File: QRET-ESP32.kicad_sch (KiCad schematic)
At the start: 3 parts

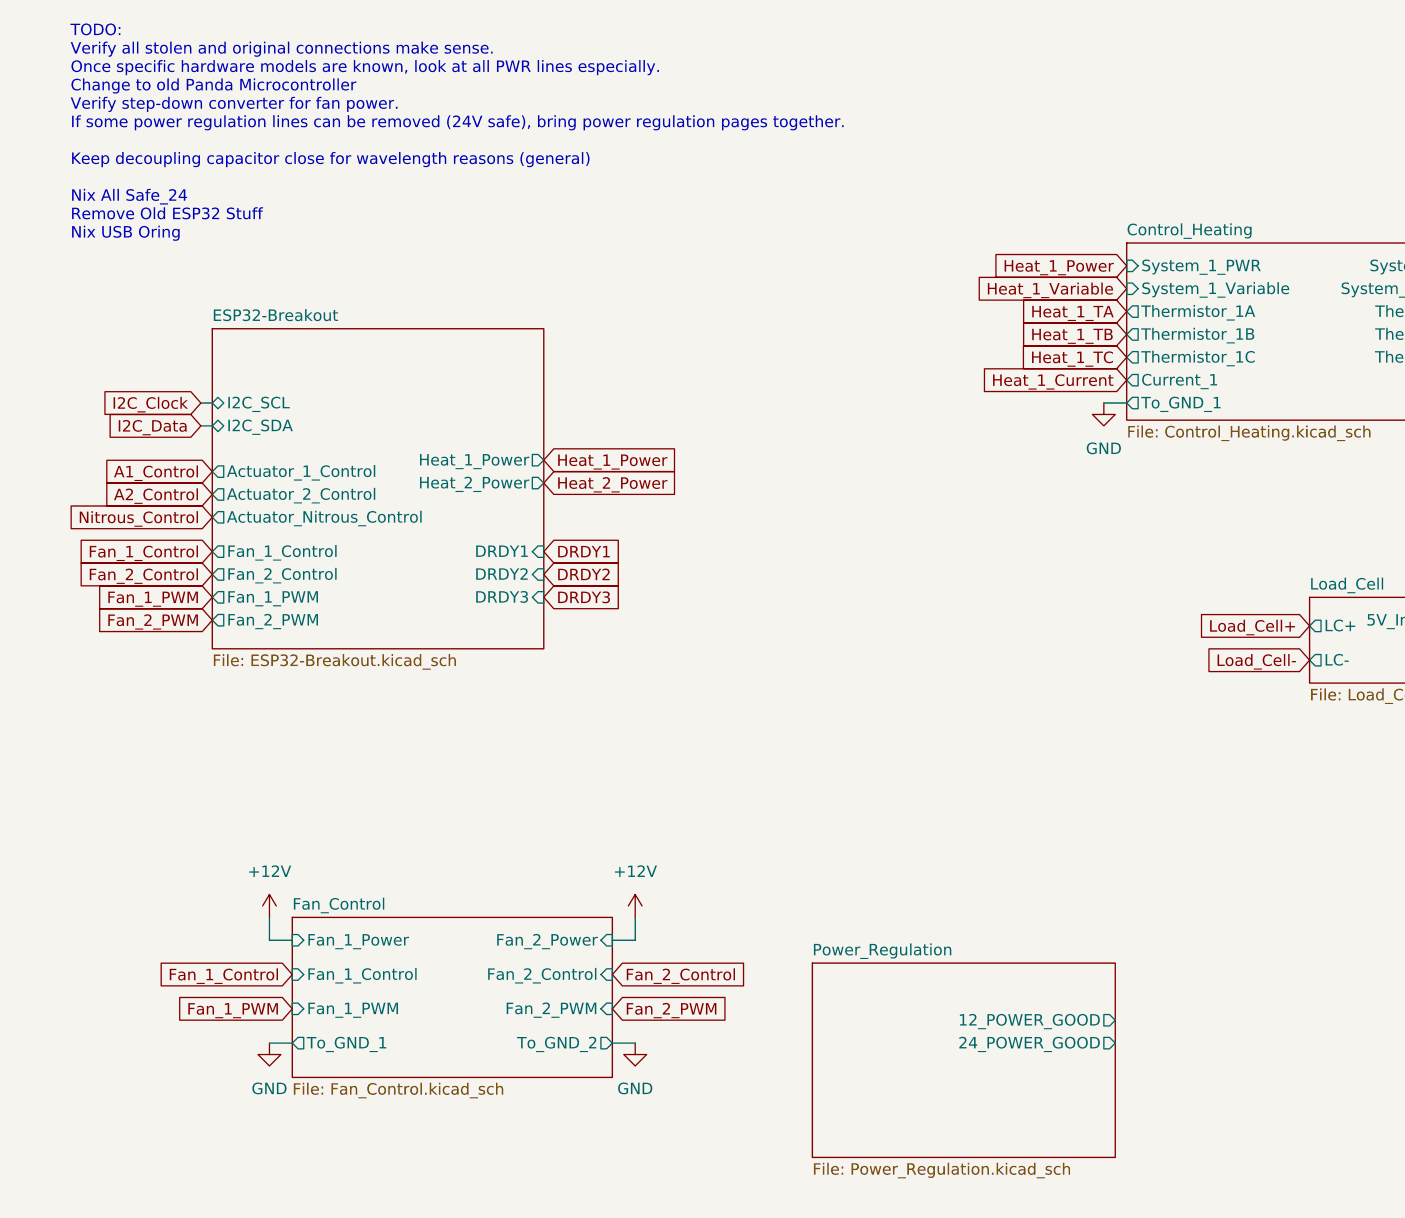
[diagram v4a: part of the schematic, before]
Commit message: Adopted 4-layer setup and organized placement
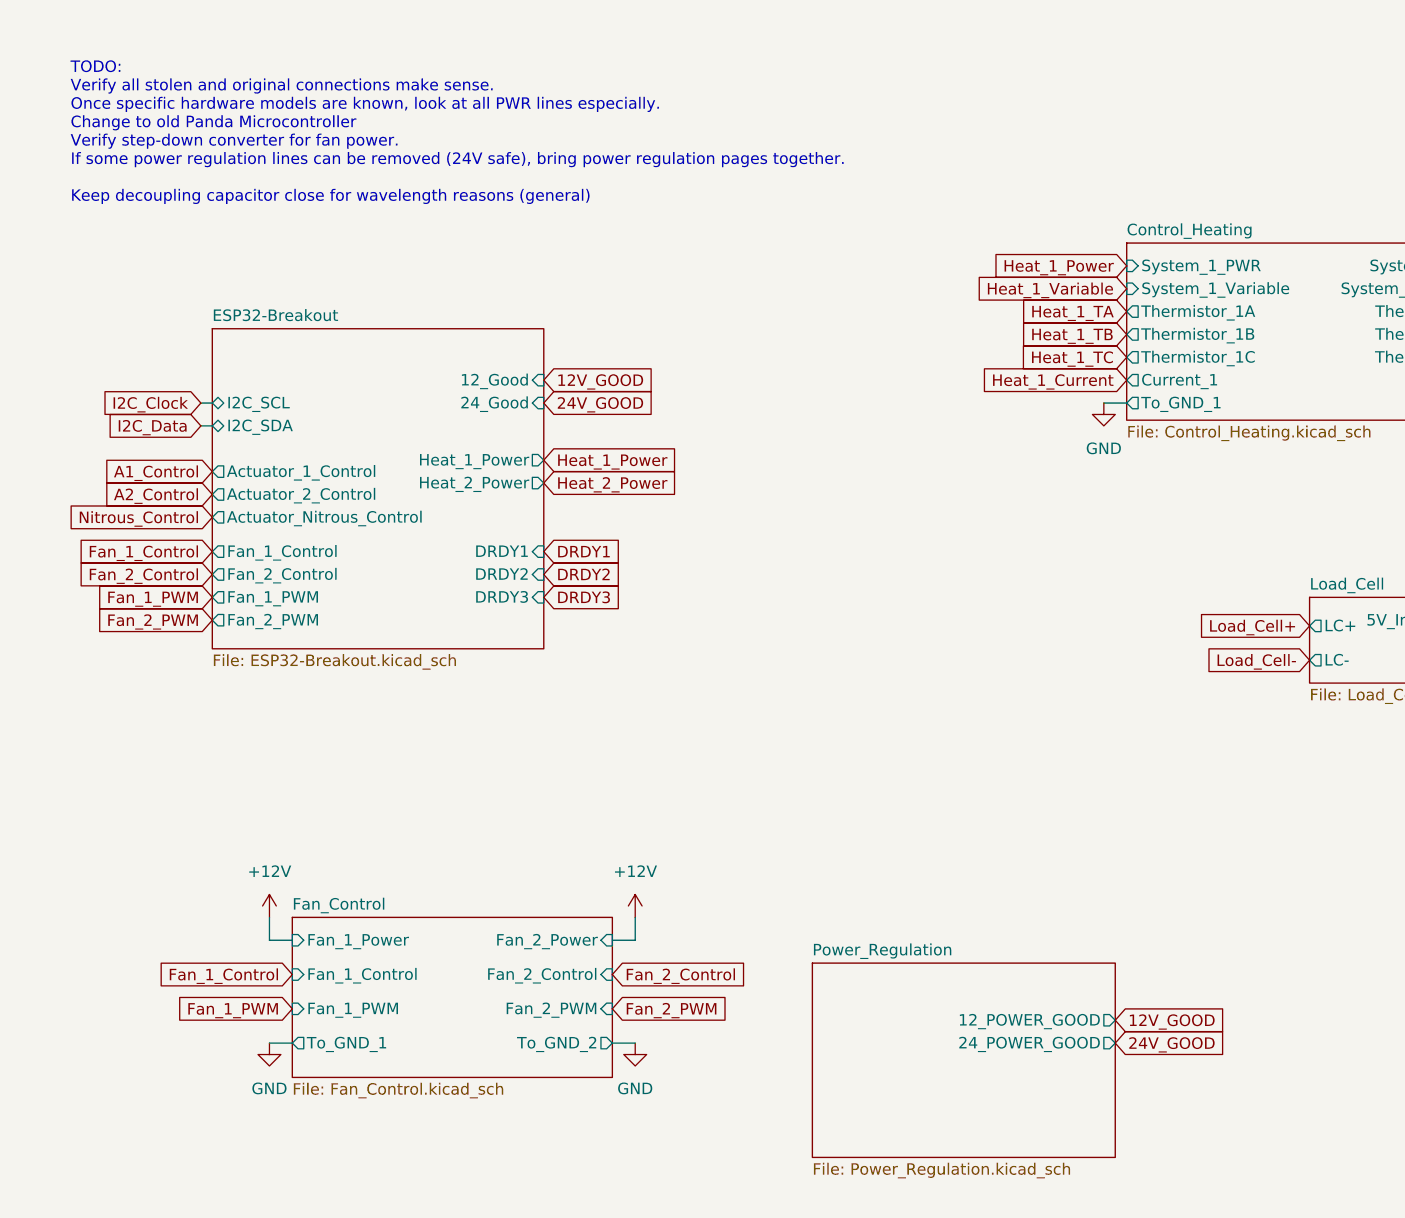
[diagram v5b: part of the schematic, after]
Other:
- sheet ESP32-Breakout ports: added 12_Good, 24_Good; removed none
- note added: "TODO: Verify all stolen and original connections make sense. Once specific hardware models are known, look at all PWR lines especially. Change to old Panda Microcontroller Verify step-down converter for fan power. If some power regulation lines can be removed (24V safe), bring power regulation pages together. Keep decoupling capacitor close for wavelength reasons (general)"
- note removed: "TODO: Verify all stolen and original connections make sense. Once specific hardware models are known, look at all PWR lines especially. Change to old Panda Microcontroller Verify step-down converter for fan power. If some power regulation lines can be removed (24V safe), bring power regulation pages together. Keep decoupling capacitor close for wavelength reasons (general) Nix All Safe_24 Remove 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"
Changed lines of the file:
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@@
 	(generator_version "9.0")
 	(paper "A4")
-	(text "TODO:\nVerify all stolen and original connections make sense.\nOnce specific hardware models are known, look at all PWR lines especially.\nChange to old Panda Microcontroller\nVerify step-down converter for fan power.\nIf some power regulation lines can be removed (24V safe), bring power regulation pages together.\n\nKeep decoupling capacitor close for wavelength reasons (general)\n\nNix All Safe_24\nRemove Old ESP32 Stuff\nNix USB Oring\n"
+	(text "TODO:\nVerify all stolen and original connections make sense.\nOnce specific hardware models are known, look at all PWR lines especially.\nChange to old Panda Microcontroller\nVerify step-down converter for fan power.\nIf some power regulation lines can be removed (24V safe), bring power regulation pages together.\n\nKeep decoupling capacitor close for wavelength reasons (general)\n"
 		(exclude_from_sim no)
 		(at 14.732 27.178 0)
@@
 		)
 	)
+	(global_label "24V_GOOD"
+		(shape input)
+		(at 130.81 128.27 0)
+		(fields_autoplaced yes)
+		(effects
+			(font
+				(size 1.27 1.27)
+			)
+			(justify left)
+		)
+		(property "Intersheetrefs" "${INTERSHEET_REFS}"
+			(at 143.4714 128.27 0)
+			(effects
+				(font
+					(size 1.27 1.27)
+				)
+				(justify left)
+				(hide yes)
+			)
+		)
+	)
 	(global_label "I2C_Data"
 		(shape input)
@@
 		)
 	)
+	(global_label "24V_GOOD"
+		(shape input)
+		(at 67.31 57.15 0)
+		(fields_autoplaced yes)
+		(effects
+			(font
+				(size 1.27 1.27)
+			)
+			(justify left)
+		)
+		(property "Intersheetrefs" "${INTERSHEET_REFS}"
+			(at 79.9714 57.15 0)
+			(effects
+				(font
+					(size 1.27 1.27)
+				)
+				(justify left)
+				(hide yes)
+			)
+		)
+	)
 	(global_label "Heat_1_Current"
 		(shape input)
@@
 		)
 	)
+	(global_label "12V_GOOD"
+		(shape input)
+		(at 67.31 54.61 0)
+		(fields_autoplaced yes)
+		(effects
+			(font
+				(size 1.27 1.27)
+			)
+			(justify left)
+		)
+		(property "Intersheetrefs" "${INTERSHEET_REFS}"
+			(at 79.9714 54.61 0)
+			(effects
+				(font
+					(size 1.27 1.27)
+				)
+				(justify left)
+				(hide yes)
+			)
+		)
+	)
 	(global_label "DRDY1"
 		(shape input)
@@
 		)
 	)
+	(global_label "12V_GOOD"
+		(shape input)
+		(at 130.81 125.73 0)
+		(fields_autoplaced yes)
+		(effects
+			(font
+				(size 1.27 1.27)
+			)
+			(justify left)
+		)
+		(property "Intersheetrefs" "${INTERSHEET_REFS}"
+			(at 143.4714 125.73 0)
+			(effects
+				(font
+					(size 1.27 1.27)
+				)
+				(justify left)
+				(hide yes)
+			)
+		)
+	)
 	(global_label "Fan_1_PWM"
 		(shape input)
@@
 			)
 		)
+		(pin "12_Good" input
+			(at 67.31 54.61 0)
+			(effects
+				(font
+					(size 1.27 1.27)
+				)
+				(justify right)
+			)
+		)
+		(pin "24_Good" input
+			(at 67.31 57.15 0)
+			(effects
+				(font
+					(size 1.27 1.27)
+				)
+				(justify right)
+			)
+		)

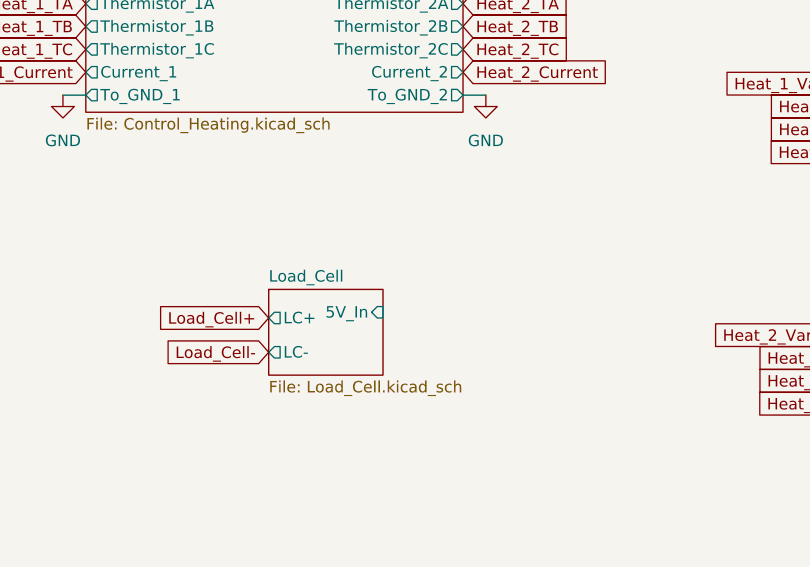
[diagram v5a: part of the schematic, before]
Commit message: Initial PCB placement and wiring.
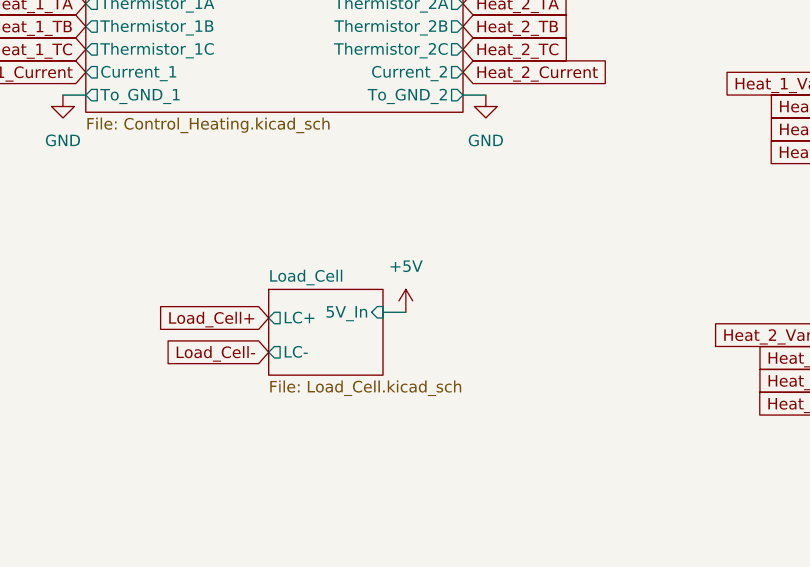
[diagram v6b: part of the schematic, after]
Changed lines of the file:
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@@
+	(wire
+		(pts
+			(xy 165.1 81.28) (xy 167.64 81.28)
+		)
+		(stroke
+			(width 0)
+			(type default)
+		)
+	)
 	(wire
 		(pts
@@
 					(unit 1)
 				)
+			)
+		)
+	)
+	(symbol
+		(lib_id "power:+5V")
+		(at 167.64 81.28 0)
+		(mirror y)
+		(unit 1)
+		(exclude_from_sim no)
+		(in_bom yes)
+		(on_board yes)
+		(dnp no)
+		(property "Reference" "#PWR01"
+			(at 167.64 85.09 0)
+			(effects
+				(font
+					(size 1.27 1.27)
+				)
+				(hide yes)
+			)
+		)
+		(property "Value" "+5V"
+			(at 167.64 76.2 0)
+			(effects
+				(font
+					(size 1.27 1.27)
+				)
+			)
+		)
+		(property "Footprint" ""
+			(at 167.64 81.28 0)
+			(effects
+				(font
+					(size 1.27 1.27)
+				)
+				(hide yes)
+			)
+		)
+		(property "Datasheet" ""
+			(at 167.64 81.28 0)
+			(effects
+				(font
+					(size 1.27 1.27)
+				)
+				(hide yes)
+			)
+		)
+		(property "Description" "Power symbol creates a global label with name \"+5V\""
+			(at 167.64 81.28 0)
+			(effects
+				(font
+					(size 1.27 1.27)
+				)
+				(hide yes)
+			)
+		)
+		(pin "1"
+		)
+		(instances
+			(project ""
+				(path "/24817451-dfe0-4b9a-9d93-7304529c9d58"
+					(reference "#PWR01")
+					(unit 1)
+				)
